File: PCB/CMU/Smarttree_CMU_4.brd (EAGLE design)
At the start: 71.1 x 45.7 mm, 43 parts, among them X2 057-006-0

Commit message: new connector on cmu
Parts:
- removed X2: 057-006-0, con-panduit:057-006-0
- added U$1: 8PINCONN, SmartTreeCan:8PINCONN
- moved C6 1.98 mm to (40.1, 31.2)
- moved R14 1.98 mm to (40.1, 28.7)
- moved Z1 1.98 mm to (36.8, 30.0)
- moved Z2 1.98 mm to (33.5, 30.0)
- moved C2 1.98 mm to (30.0, 31.2)
- moved R13 1.98 mm to (30.0, 28.7)
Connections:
- net CSI: now also U$1.4; no longer X2.5
- net CSO: now also U$1.2; no longer X2.8
- net GND: now also U$1.1; no longer X2.7
- net RELAY_IN: now also U$1.3; no longer X2.6
- net RELAY_OUT: now also U$1.5; no longer X2.4
- net TS: now also U$1.6; no longer X2.3
- net VCC: now also U$1.8; no longer X2.1
- net VS: now also U$1.7; no longer X2.2
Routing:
- net CSO: track 27.2 -> 37.8 mm
- net RELAY_OUT: track 38.8 -> 34.2 mm
- net VS: track 39.2 -> 34.8 mm
- net CSI: track 26.0 -> 29.4 mm, vias 1 -> 0
- net RELAY_IN: track 16.8 -> 14.1 mm
- net TS: track 19.5 -> 18.7 mm
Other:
- board size 71.1 x 45.7 mm -> 71.1 x 48.3 mm

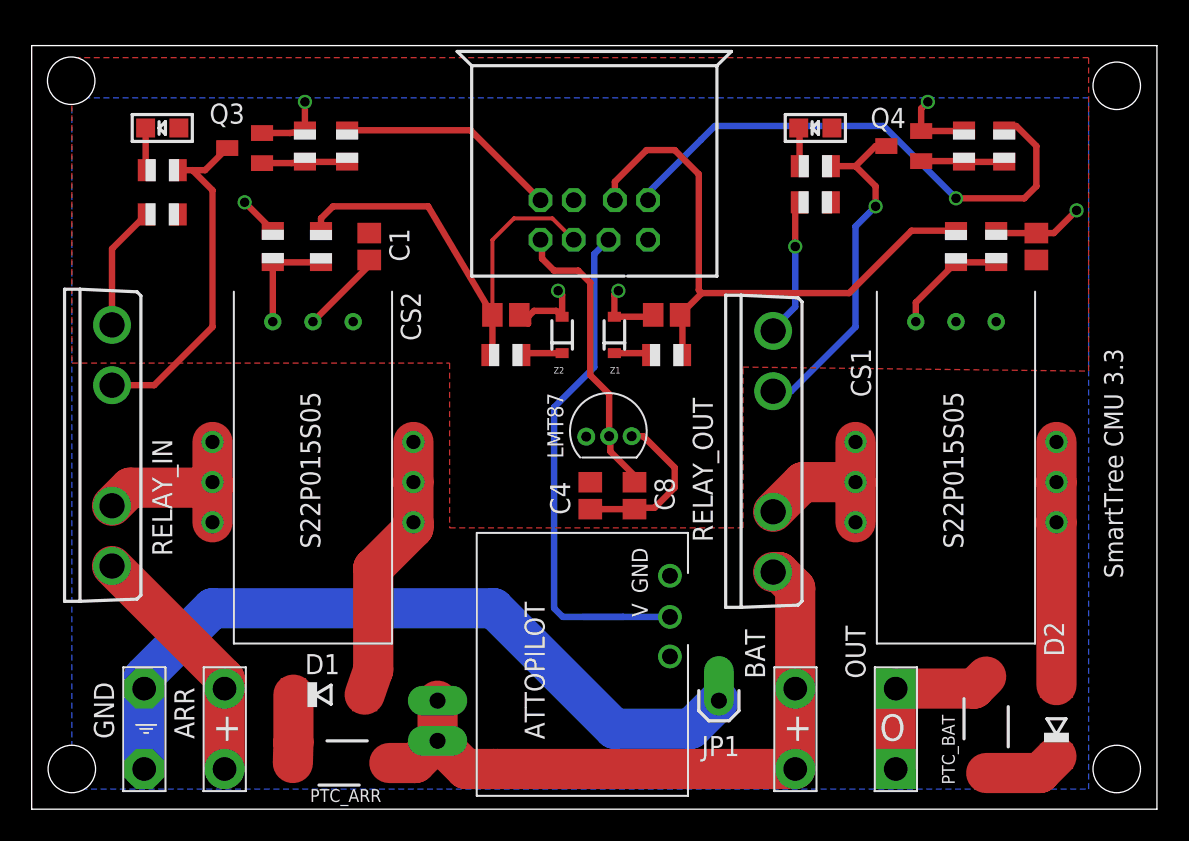
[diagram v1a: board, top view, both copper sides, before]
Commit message: gerber cmu with new connector footprint
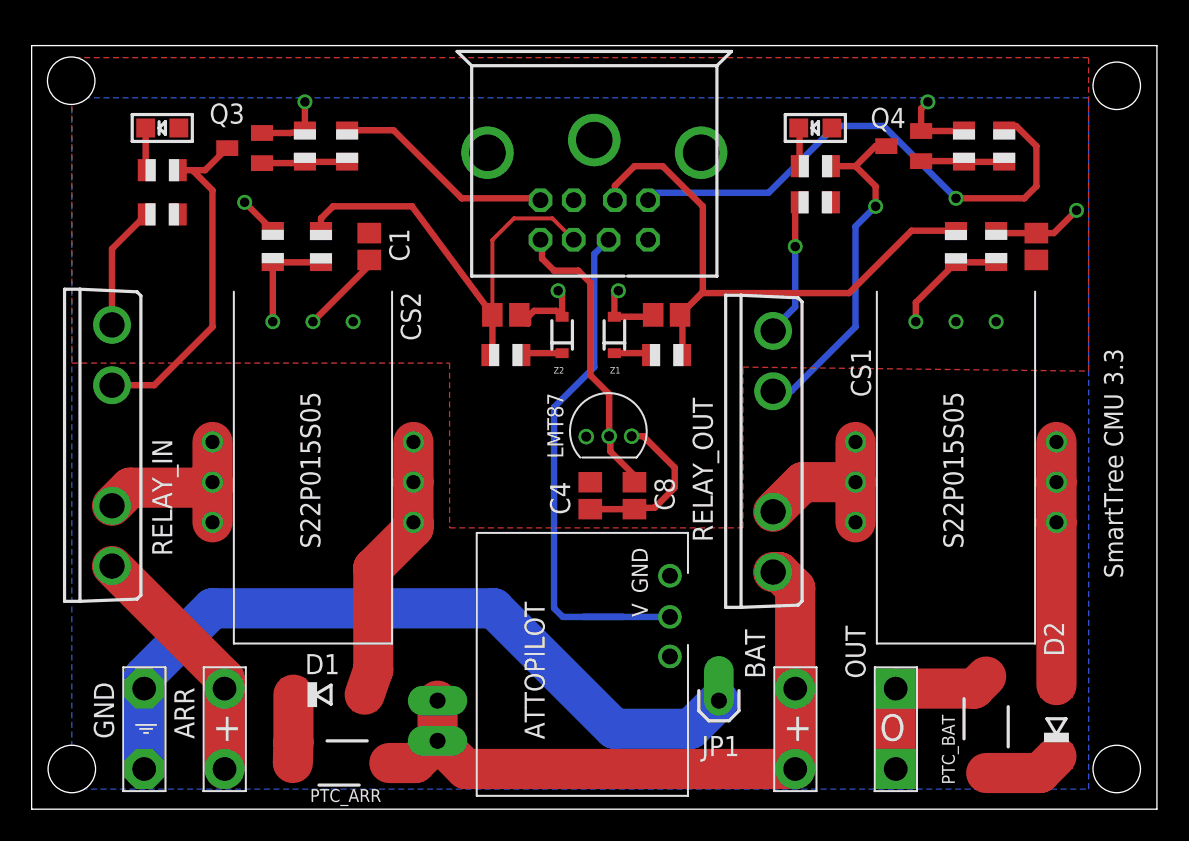
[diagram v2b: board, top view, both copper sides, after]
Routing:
- net CSO: track 37.8 -> 36.2 mm
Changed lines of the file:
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@@
 </class>
 </classes>
-<designrules name="SeeedStudio_2layer_DRU_no_angle_20140221">
+<designrules name="LaenPCBOrder">
 <description language="de">&lt;b&gt;EAGLE Design Rules&lt;/b&gt;
 &lt;p&gt;
@@
 Einstellungen hier und speichern die Design Rules unter
 einem neuen Namen ab.</description>
-<description language="en">&lt;b&gt;EAGLE Design Rules&lt;/b&gt;
+<description language="en">&lt;b&gt;Laen's PCB Order Design Rules&lt;/b&gt;
 &lt;p&gt;
-The default Design Rules have been set to cover
-a wide range of applications. Your particular design
-may have different requirements, so please make the
-necessary adjustments and save your customized
-design rules under a new name.</description>
-<description language="zh">&lt;b&gt;Seeed Studio EAGLE Design Rules&lt;/b&gt;
-</description>
+Please make sure your boards conform to these design rules.</description>
 <param name="layerSetup" value="(1*16)"/>
-<param name="mtCopper" value="0.035mm 0.0175mm 0.035mm 0.035mm 0.035mm 0.035mm 0.035mm 0.035mm 0.035mm 0.035mm 0.035mm 0.035mm 0.035mm 0.035mm 0.0175mm 0.035mm"/>
-<param name="mtIsolate" value="1.5mm 1.1mm 0.2mm 0.15mm 0.2mm 0.15mm 0.2mm 0.15mm 0.2mm 0.15mm 0.2mm 0.15mm 0.2mm 0.15mm 0.2mm"/>
+<param name="mtCopper" value="0.0356mm 0.0356mm 0.0356mm 0.0356mm 0.0356mm 0.0356mm 0.0356mm 0.0356mm 0.0356mm 0.0356mm 0.0356mm 0.0356mm 0.0356mm 0.0356mm 0.0356mm 0.0356mm"/>
+<param name="mtIsolate" value="1.5011mm 0.1499mm 0.2007mm 0.1499mm 0.2007mm 0.1499mm 0.2007mm 0.1499mm 0.2007mm 0.1499mm 0.2007mm 0.1499mm 0.2007mm 0.1499mm 0.2007mm"/>
 <param name="mdWireWire" value="6mil"/>
 <param name="mdWirePad" value="6mil"/>
@@
 <param name="mdPadVia" value="6mil"/>
 <param name="mdViaVia" value="6mil"/>
-<param name="mdSmdPad" value="0mil"/>
-<param name="mdSmdVia" value="0mil"/>
-<param name="mdSmdSmd" value="0mil"/>
+<param name="mdSmdPad" value="6mil"/>
+<param name="mdSmdVia" value="6mil"/>
+<param name="mdSmdSmd" value="6mil"/>
 <param name="mdViaViaSameLayer" value="8mil"/>
 <param name="mnLayersViaInSmd" value="2"/>
-<param name="mdCopperDimension" value="10mil"/>
-<param name="mdDrill" value="10mil"/>
+<param name="mdCopperDimension" value="15mil"/>
+<param name="mdDrill" value="6mil"/>
 <param name="mdSmdStop" value="0mil"/>
 <param name="msWidth" value="6mil"/>
-<param name="msDrill" value="12mil"/>
-<param name="msMicroVia" value="12mil"/>
+<param name="msDrill" value="13mil"/>
+<param name="msMicroVia" value="13mil"/>
 <param name="msBlindViaRatio" value="0.5"/>
 <param name="rvPadTop" value="0.25"/>
@@
 <param name="rvMicroViaOuter" value="0.25"/>
 <param name="rvMicroViaInner" value="0.25"/>
-<param name="rlMinPadTop" value="10mil"/>
+<param name="rlMinPadTop" value="7mil"/>
 <param name="rlMaxPadTop" value="20mil"/>
-<param name="rlMinPadInner" value="10mil"/>
+<param name="rlMinPadInner" value="7mil"/>
 <param name="rlMaxPadInner" value="20mil"/>
-<param name="rlMinPadBottom" value="10mil"/>
+<param name="rlMinPadBottom" value="7mil"/>
 <param name="rlMaxPadBottom" value="20mil"/>
-<param name="rlMinViaOuter" value="6mil"/>
+<param name="rlMinViaOuter" value="7mil"/>
 <param name="rlMaxViaOuter" value="20mil"/>
-<param name="rlMinViaInner" value="6mil"/>
+<param name="rlMinViaInner" value="7mil"/>
 <param name="rlMaxViaInner" value="20mil"/>
 <param name="rlMinMicroViaOuter" value="4mil"/>
@@
 <param name="psTop" value="-1"/>
 <param name="psBottom" value="-1"/>
-<param name="psFirst" value="0"/>
+<param name="psFirst" value="-1"/>
 <param name="psElongationLong" value="100"/>
 <param name="psElongationOffset" value="100"/>
 <param name="mvStopFrame" value="1"/>
 <param name="mvCreamFrame" value="0"/>
-<param name="mlMinStopFrame" value="2mil"/>
-<param name="mlMaxStopFrame" value="2mil"/>
+<param name="mlMinStopFrame" value="3mil"/>
+<param name="mlMaxStopFrame" value="3mil"/>
 <param name="mlMinCreamFrame" value="0mil"/>
 <param name="mlMaxCreamFrame" value="0mil"/>
-<param name="mlViaStopLimit" value="100mil"/>
+<param name="mlViaStopLimit" value="0mil"/>
 <param name="srRoundness" value="0"/>
 <param name="srMinRoundness" value="0mil"/>
@@
 <param name="checkAngle" value="0"/>
 <param name="checkFont" value="1"/>
-<param name="checkRestrict" value="0"/>
+<param name="checkRestrict" value="1"/>
 <param name="useDiameter" value="13"/>
 <param name="maxErrors" value="50"/>
@@
 <contactref element="U$1" pad="2"/>
 <wire x1="51.666" y1="32.616" x2="42.356" y2="32.616" width="0.4064" layer="1"/>
-<wire x1="42.356" y1="32.616" x2="40.982" y2="31.242" width="0.4064" layer="1"/>
-<wire x1="36.86" y1="38.49" x2="36.86" y2="39.654" width="0.4064" layer="1"/>
-<wire x1="36.86" y1="39.654" x2="38.862" y2="41.656" width="0.4064" layer="1"/>
-<wire x1="38.862" y1="41.656" x2="40.64" y2="41.656" width="0.4064" layer="1"/>
-<wire x1="40.64" y1="41.656" x2="42.164" y2="40.132" width="0.4064" layer="1"/>
-<wire x1="42.164" y1="40.132" x2="42.164" y2="32.808" width="0.4064" layer="1"/>
-<wire x1="42.164" y1="32.808" x2="42.356" y2="32.616" width="0.4064" layer="1"/>
+<wire x1="42.356" y1="32.616" x2="42.081" y2="32.341" width="0.4064" layer="1"/>
+<wire x1="42.081" y1="32.341" x2="40.982" y2="31.242" width="0.4064" layer="1"/>
+<wire x1="36.86" y1="38.49" x2="36.86" y2="39.4" width="0.4064" layer="1"/>
+<wire x1="36.86" y1="39.4" x2="38.1" y2="40.64" width="0.4064" layer="1"/>
+<wire x1="38.1" y1="40.64" x2="39.878" y2="40.64" width="0.4064" layer="1"/>
+<wire x1="39.878" y1="40.64" x2="42.418" y2="38.1" width="0.4064" layer="1"/>
+<wire x1="42.418" y1="38.1" x2="42.418" y2="32.678" width="0.4064" layer="1"/>
+<wire x1="42.418" y1="32.678" x2="42.081" y2="32.341" width="0.4064" layer="1"/>
 </signal>
 <signal name="VCC">
@@
 <contactref element="R3" pad="2"/>
 <contactref element="U$1" pad="3"/>
-<wire x1="19.939" y1="42.91" x2="27.74" y2="42.91" width="0.4064" layer="1"/>
-<wire x1="27.74" y1="42.91" x2="32.16" y2="38.49" width="0.4064" layer="1"/>
+<wire x1="19.939" y1="42.91" x2="22.876" y2="42.91" width="0.4064" layer="1"/>
+<wire x1="22.876" y1="42.91" x2="27.178" y2="38.608" width="0.4064" layer="1"/>
+<wire x1="27.178" y1="38.608" x2="32.042" y2="38.608" width="0.4064" layer="1"/>
+<wire x1="32.042" y1="38.608" x2="32.16" y2="38.49" width="0.4064" layer="1"/>
 </signal>
 <signal name="RELAY_OUT">
@@
 <wire x1="61.738" y1="43.18" x2="61.468" y2="42.91" width="0.4064" layer="1"/>
 <contactref element="U$1" pad="5"/>
-<wire x1="42.3" y1="42.3" x2="43.18" y2="43.18" width="0.4064" layer="16"/>
-<wire x1="43.18" y1="43.18" x2="53.848" y2="43.18" width="0.4064" layer="16"/>
 <wire x1="38.96" y1="38.49" x2="38.96" y2="38.96" width="0.4064" layer="16"/>
-<wire x1="38.96" y1="38.96" x2="42.3" y2="42.3" width="0.4064" layer="16"/>
+<wire x1="38.96" y1="38.96" x2="46.58" y2="38.96" width="0.4064" layer="16"/>
+<wire x1="46.58" y1="38.96" x2="50.8" y2="43.18" width="0.4064" layer="16"/>
+<wire x1="50.8" y1="43.18" x2="53.848" y2="43.18" width="0.4064" layer="16"/>
 </signal>
 <signal name="N$2">
@@
 <wire x1="18.288" y1="36.56" x2="18.288" y2="37.338" width="0.4064" layer="1"/>
 <wire x1="18.288" y1="37.338" x2="19.05" y2="38.1" width="0.4064" layer="1"/>
-<wire x1="19.05" y1="38.1" x2="25.058" y2="38.1" width="0.4064" layer="1"/>
-<wire x1="25.058" y1="38.1" x2="29.122" y2="31.242" width="0.4064" layer="1"/>
+<wire x1="19.05" y1="38.1" x2="24.042" y2="38.1" width="0.4064" layer="1"/>
+<wire x1="24.042" y1="38.1" x2="29.122" y2="31.242" width="0.4064" layer="1"/>
 <contactref element="R13" pad="1"/>
 <wire x1="29.122" y1="31.242" x2="29.122" y2="28.852" width="0.4064" layer="1"/>

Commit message: revise resistor value for current sensor
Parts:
- R10: value 1k -> 10k
- R11: value 1k -> 330
- R12: value 10k -> 330
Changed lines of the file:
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@@
 <attribute name="VALUE" x="24.765" y="32.258" size="1.27" layer="27"/>
 </element>
-<element name="R10" library="adafruit" package="R0805" value="1k" x="15.24" y="35.56" smashed="yes" rot="R270">
+<element name="R10" library="adafruit" package="R0805" value="10k" x="15.24" y="35.56" smashed="yes" rot="R270">
 <attribute name="VALUE" x="12.894" y="36.442" size="1.27" layer="27" rot="R270"/>
 </element>
@@
 <attribute name="VALUE" x="38.227" y="28.956" size="0.4064" layer="27" rot="R90"/>
 </element>
-<element name="R11" library="adafruit" package="R0805" value="1k" x="58.42" y="35.56" smashed="yes" rot="R90">
+<element name="R11" library="adafruit" package="R0805" value="330" x="58.42" y="35.56" smashed="yes" rot="R90">
 <attribute name="VALUE" x="55.88" y="35.814" size="1.27" layer="27" rot="R270"/>
 </element>
-<element name="R12" library="adafruit" package="R0805" value="10k" x="18.288" y="35.56" smashed="yes" rot="R90">
+<element name="R12" library="adafruit" package="R0805" value="330" x="18.288" y="35.56" smashed="yes" rot="R90">
 <attribute name="VALUE" x="19.116" y="36.922" size="1.27" layer="27" rot="R270"/>
 </element>
